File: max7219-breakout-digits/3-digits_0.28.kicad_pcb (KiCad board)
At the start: 2 copper layers, 47.8 x 10.7 mm, 5 parts, among them J1 Conn_02x08_Odd_Even, U1 7Segment 3 digit common catho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

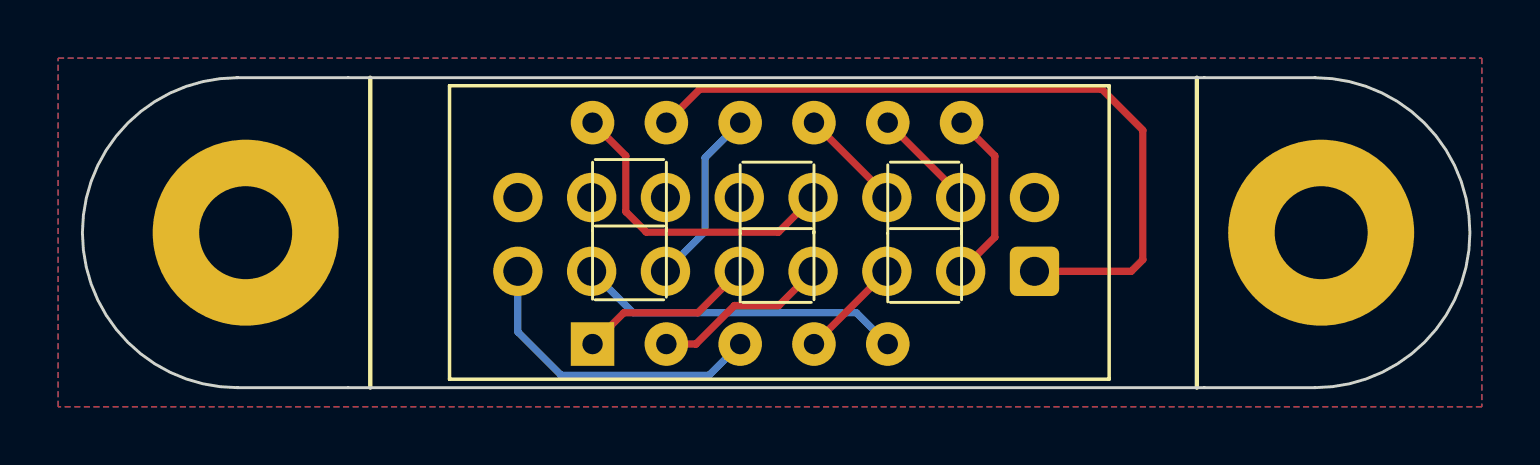
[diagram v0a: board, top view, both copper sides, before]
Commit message: rotate IDC on 0.28 displays, plated mounting holes for 0.35 displays, set version for 0.35 displays
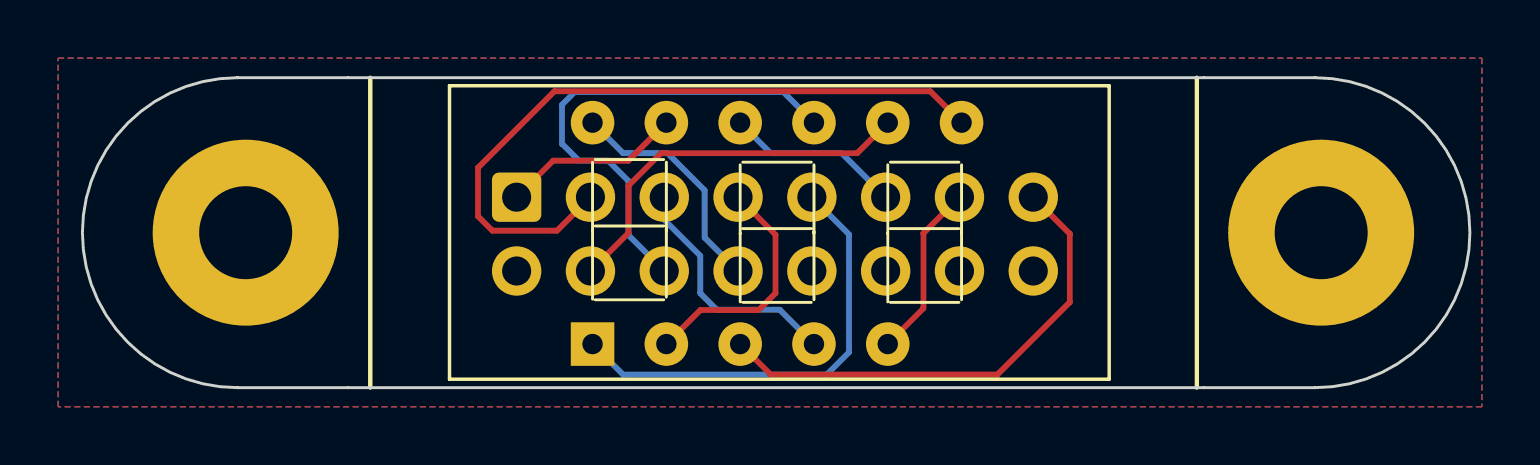
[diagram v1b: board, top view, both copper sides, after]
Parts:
- moved J1 18.0 mm to (99.8, 62.8), turned to -90 degrees
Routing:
- net /A: track 25.8 -> 6.22 mm
- net /B: track 6.08 -> 24.4 mm
- net /DIG1: track 3.62 -> 17.1 mm
- net /DIG0: track 3.62 -> 13.3 mm
- net /E: track 6.09 -> 15.4 mm
- net /DP: track 10.8 -> 16.9 mm
- net /G: track 11.2 -> 6.08 mm
- net /C: track 3.55 -> 8.46 mm
- net /DIG2: track 10.8 -> 8.08 mm
- net /D: track 6.09 -> 8.32 mm

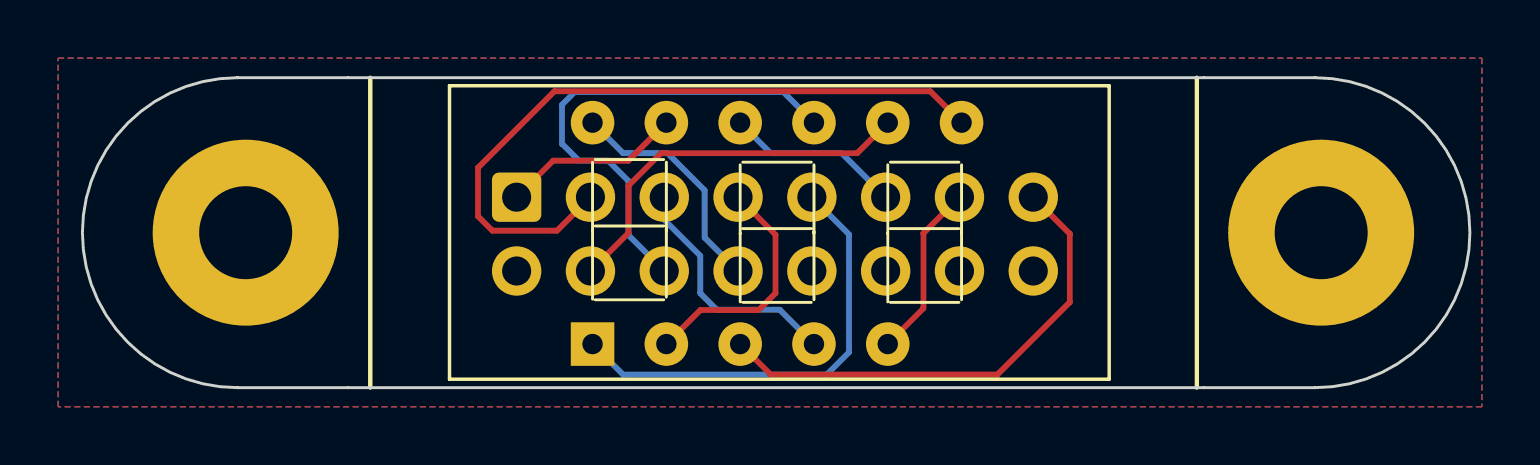
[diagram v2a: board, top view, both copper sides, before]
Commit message: add additional labels on front on backside from all boards
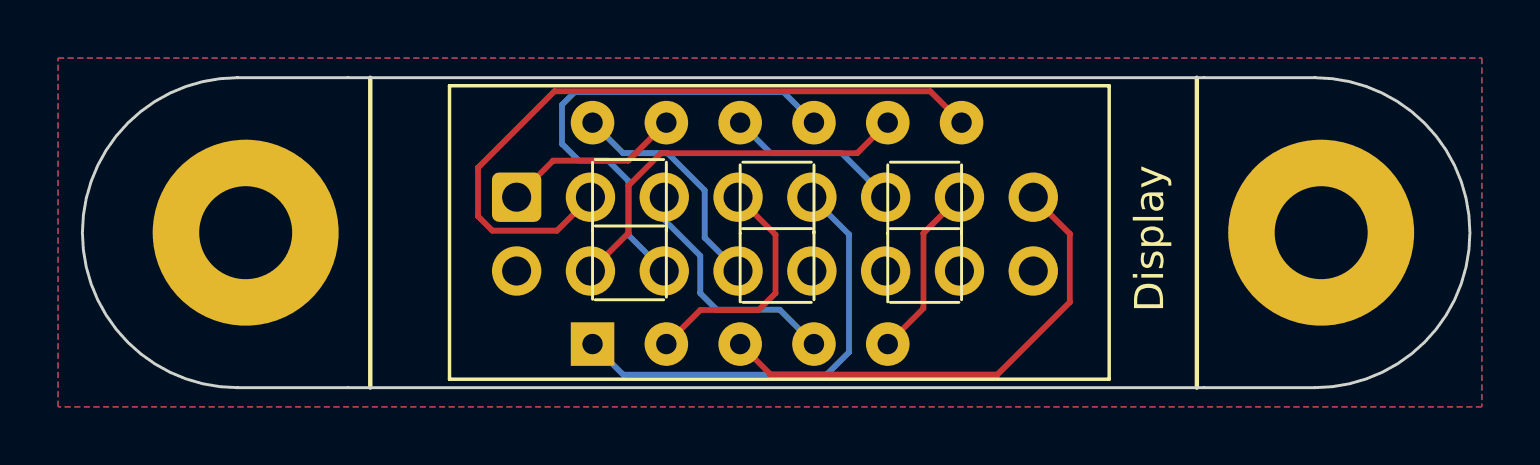
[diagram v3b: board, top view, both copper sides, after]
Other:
- board text added: "Display"
- board text added: "IDC"
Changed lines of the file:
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@@
 		(layer "Edge.Cuts")
+	)
+	(gr_text "Display"
+		(at 122.15 66.74 90)
+		(layer "F.SilkS" knockout)
+		(effects
+			(font
+				(size 1 1)
+				(thickness 0.15)
+			)
+			(justify left bottom)
+		)
+	)
+	(gr_text "IDC"
+		(at 98.6 61.35681 90)
+		(layer "B.SilkS" knockout)
+		(effects
+			(font
+				(size 2 2)
+				(thickness 0.25)
+			)
+			(justify left bottom mirror)
+		)
 	)
 	(gr_text "MobiFlight Display System 3 Digits ${REVISION}"
